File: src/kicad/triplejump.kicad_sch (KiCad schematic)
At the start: 21 parts, among them SW1 SW_Push_45deg, SW10 SW_Push_45deg, SW11 SW_Push_45deg, SW12 SW_Push_45deg, SW13 SW_Push_45deg, SW14 SW_Push_45deg, SW15 SW_Push_45deg, SW16 SW_Push_45deg, SW17 SW_Push_45deg, SW18 SW_Push_45deg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

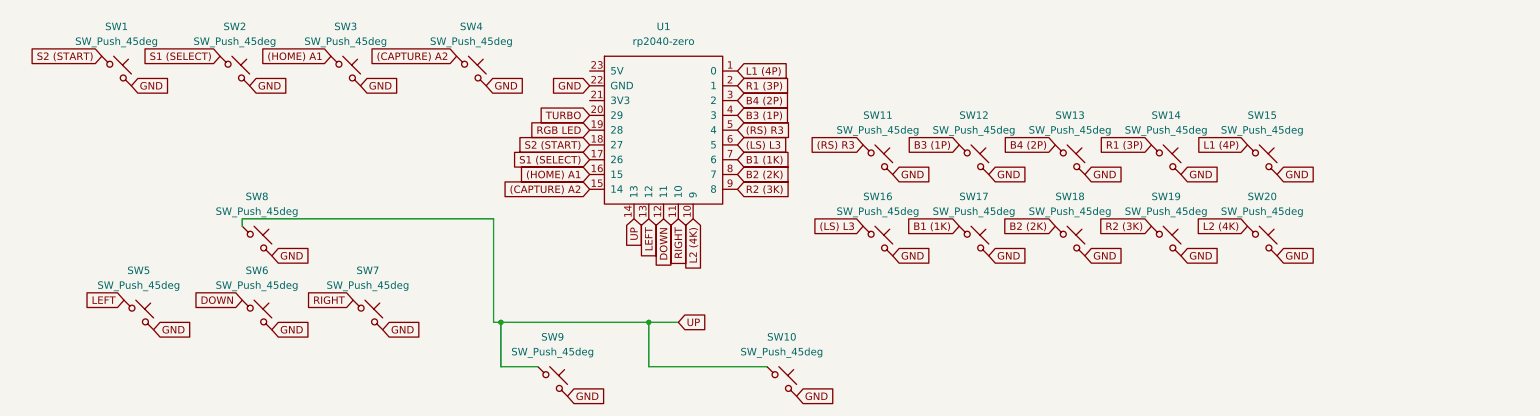
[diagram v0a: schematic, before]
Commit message: Updated PCB for version 2
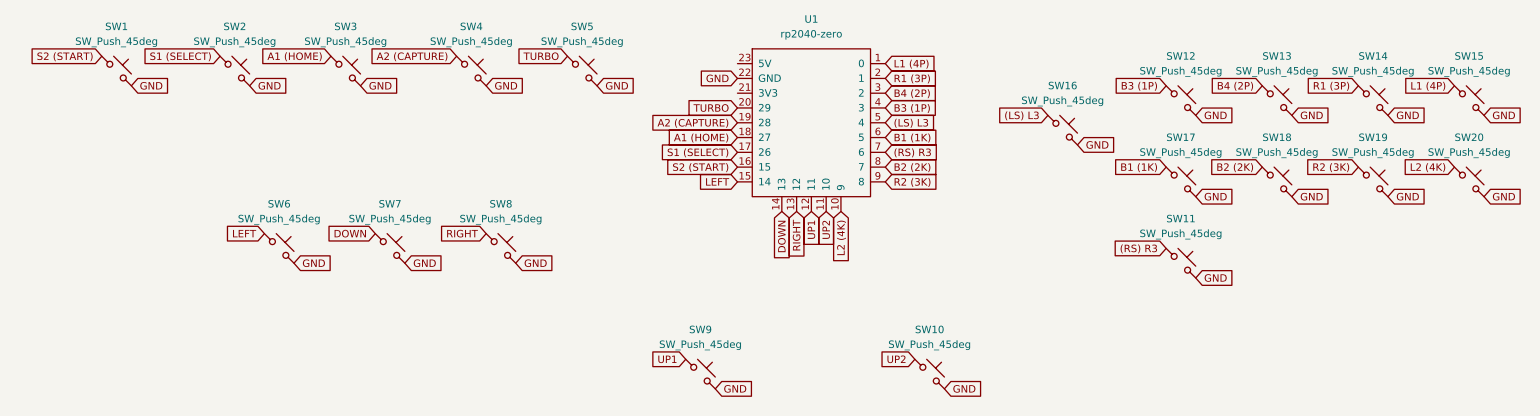
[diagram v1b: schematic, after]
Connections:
- net RGB LED is gone; now on net A2 (CAPTURE): U1.19 (28)
- net (LS) L3: now also U1.5 (4); no longer U1.6 (5)
- net (RS) R3: now also U1.7 (6); no longer U1.5 (4)
- net B1 (1K): now also U1.6 (5); no longer U1.7 (6)
- net DOWN: now also SW7.1, U1.14 (13); no longer SW6.1, U1.12 (11)
- net LEFT: now also SW6.1, U1.15 (14); no longer SW5.1, U1.13 (12)
- net RIGHT: now also SW8.1, U1.13 (12); no longer SW7.1, U1.11 (10)
- net S2 (START): now also U1.16 (15); no longer U1.18 (27)
- net TURBO: now also SW5.1
- net (CAPTURE) A2 renamed A2 (CAPTURE)
- net A2 (CAPTURE): no longer U1.15 (14)
- net (HOME) A1 renamed A1 (HOME)
- net A1 (HOME): now also U1.18 (27); no longer U1.16 (15)
- removed net UP: SW10.1, SW8.1, SW9.1, U1.14 (13)
- new net UP1: SW9.1, U1.12 (11)
- new net UP2: SW10.1, U1.11 (10)
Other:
- moved on the sheet: SW10, SW11, SW12, SW13, SW14, SW15, SW16, SW17, SW18, SW19, SW20, SW5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
